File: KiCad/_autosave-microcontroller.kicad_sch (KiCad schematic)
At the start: 5 parts, among them J1 Debugger, SW1 Reset switch, U1 STM32F051C6Tx

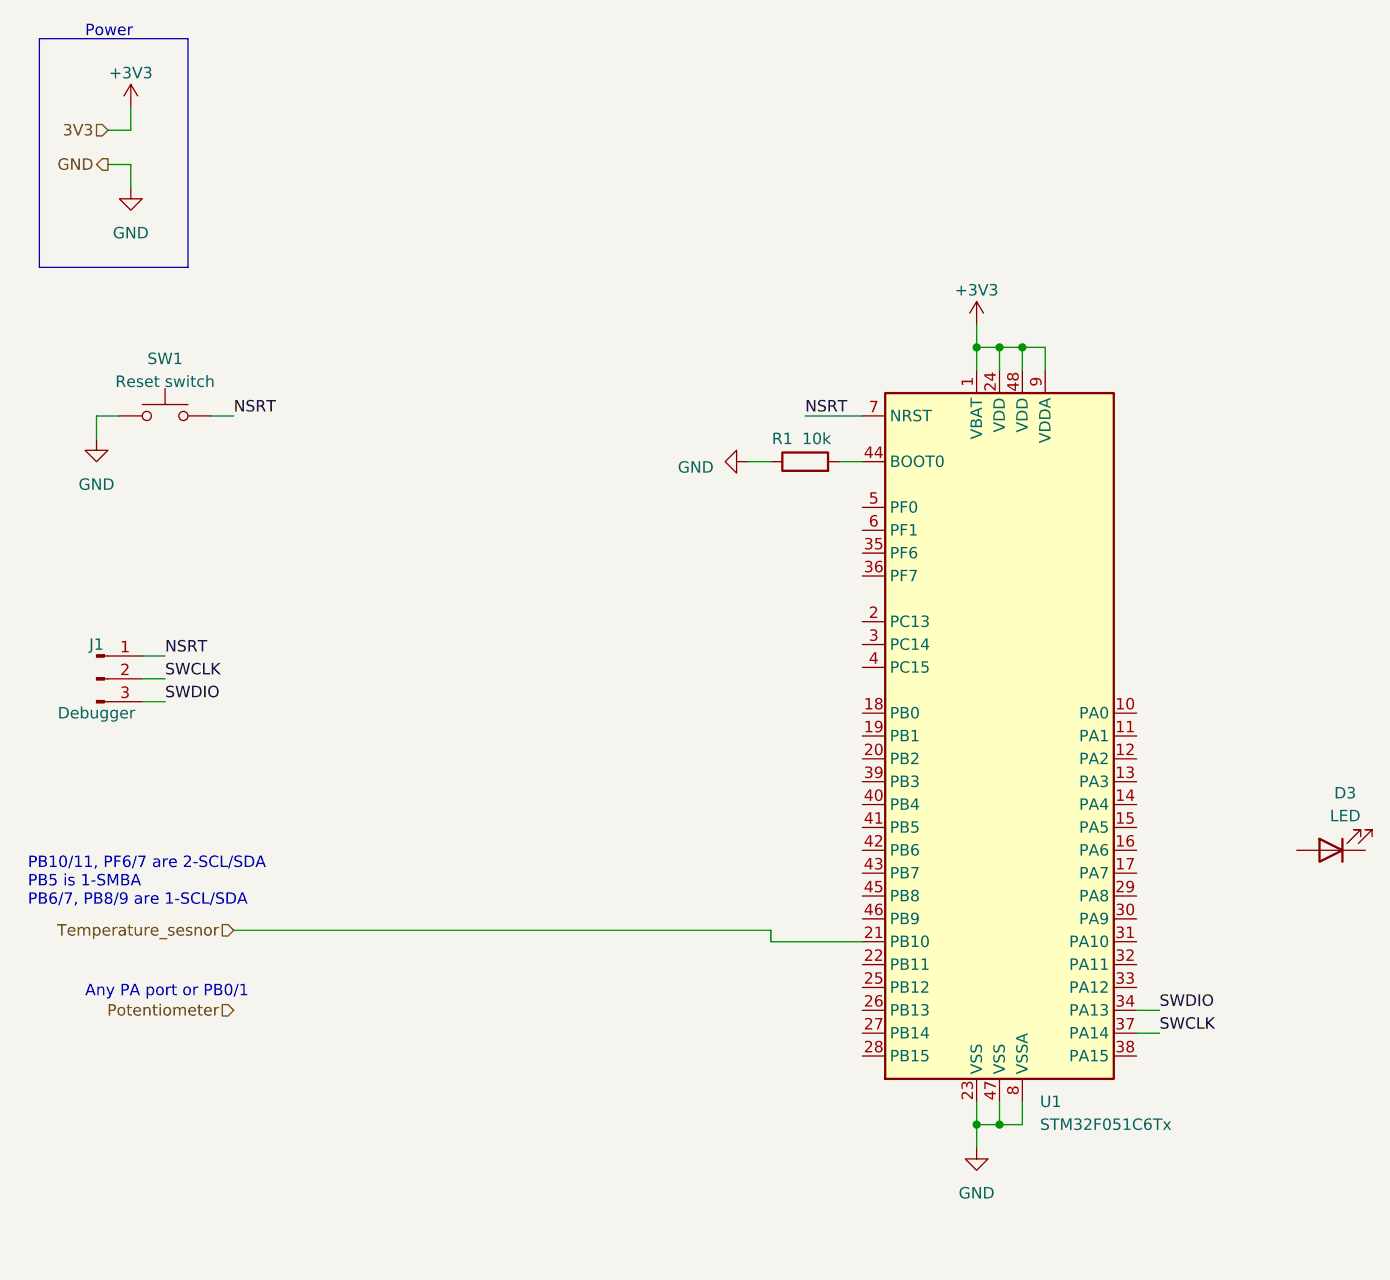
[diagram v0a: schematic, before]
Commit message: updated BOM with microcontoller
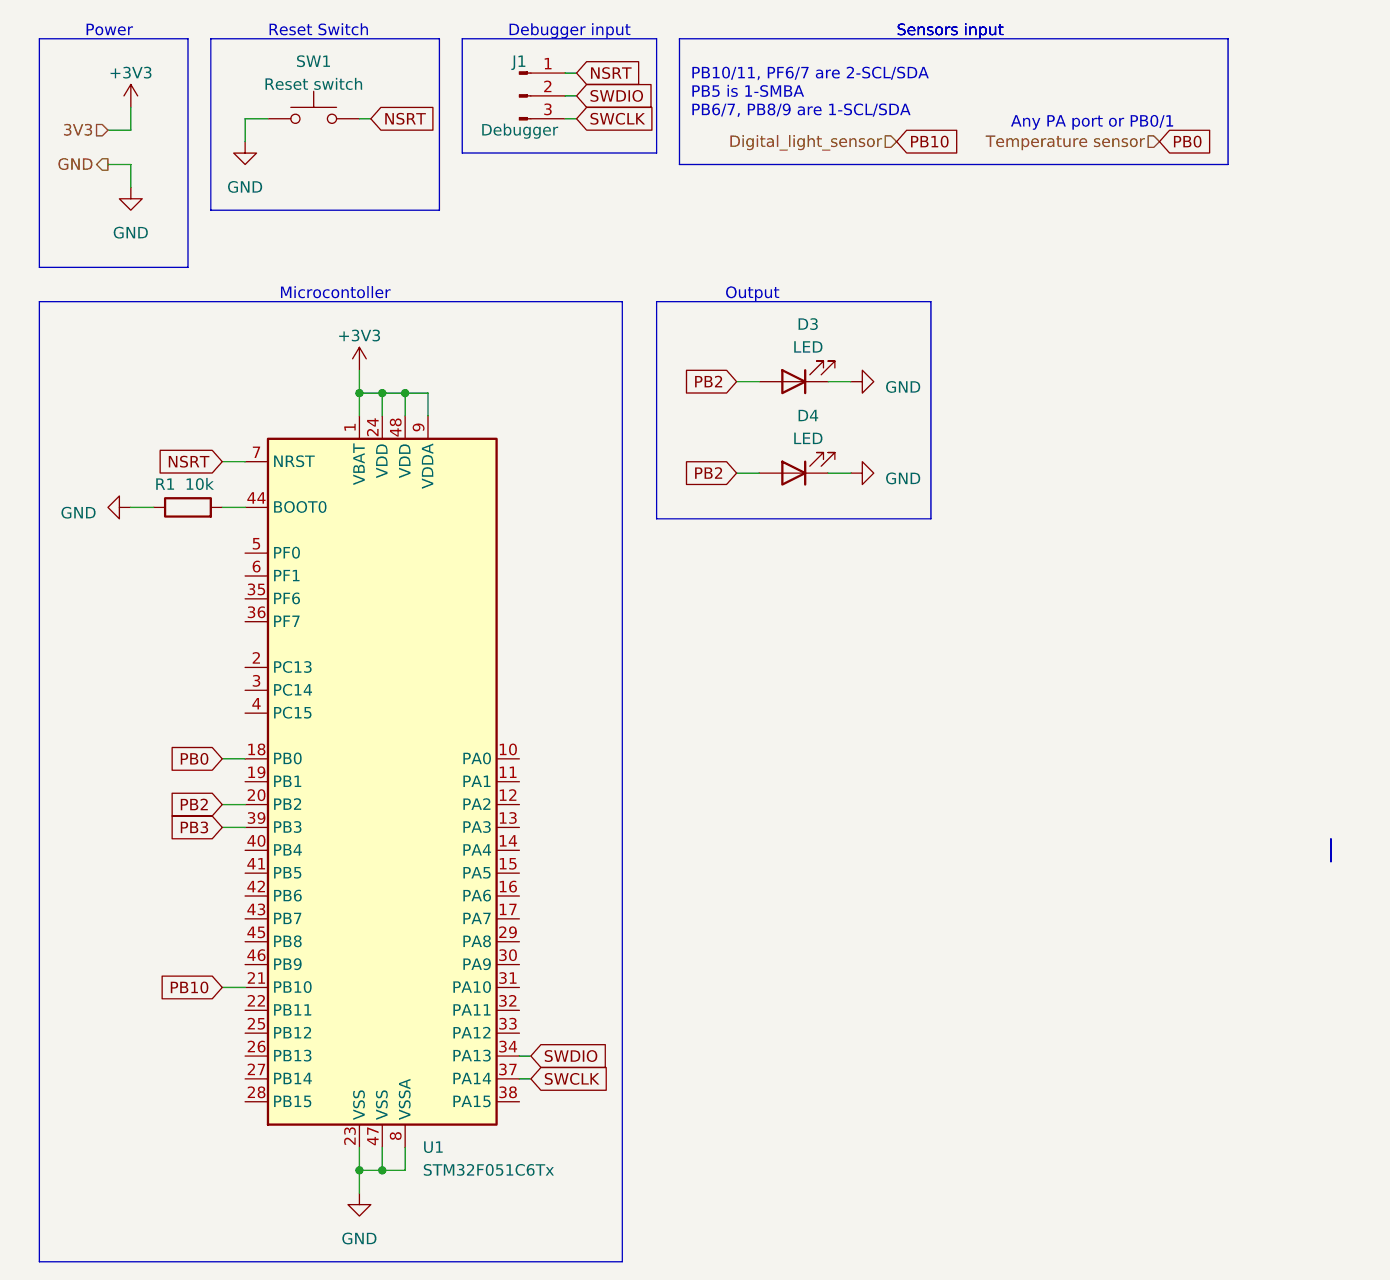
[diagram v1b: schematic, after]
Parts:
- added D4: LED, symbol Device:LED
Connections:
- net GND: now also D3.1 (K), D4.1 (K)
- net SWCLK: now also J1.3 (Pin_3); no longer J1.2 (Pin_2)
- net SWDIO: now also J1.2 (Pin_2); no longer J1.3 (Pin_3)
- net PB2: now reaches D3.2 (A)
- net PB2: now also U1.20 (PB2), D4.2 (A)
- net PB0: now reaches U1.18 (PB0)
- net PB3: now reaches U1.39 (PB3)
- net Temperature_sesnor renamed PB10
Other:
- note added: "Debugger input"
- note added: "Microcontoller"
- note added: "Output"
- note added: "Reset Switch"
- note added: "Sensors input"
- moved on the sheet: D3, J1, R1, SW1, U1
